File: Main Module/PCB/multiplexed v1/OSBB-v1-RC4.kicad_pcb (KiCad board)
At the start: 2 copper layers, 85.6 x 47.3 mm, 86 parts, among them P1 AUX 0-5V, P14 EXTRA Pins, P2 VUSB, P3 +3.3V, P4 Pit, P5 Encoders, P6 BTN 1-32, Q1 NPN, Q2 NPN, Q3 NPN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

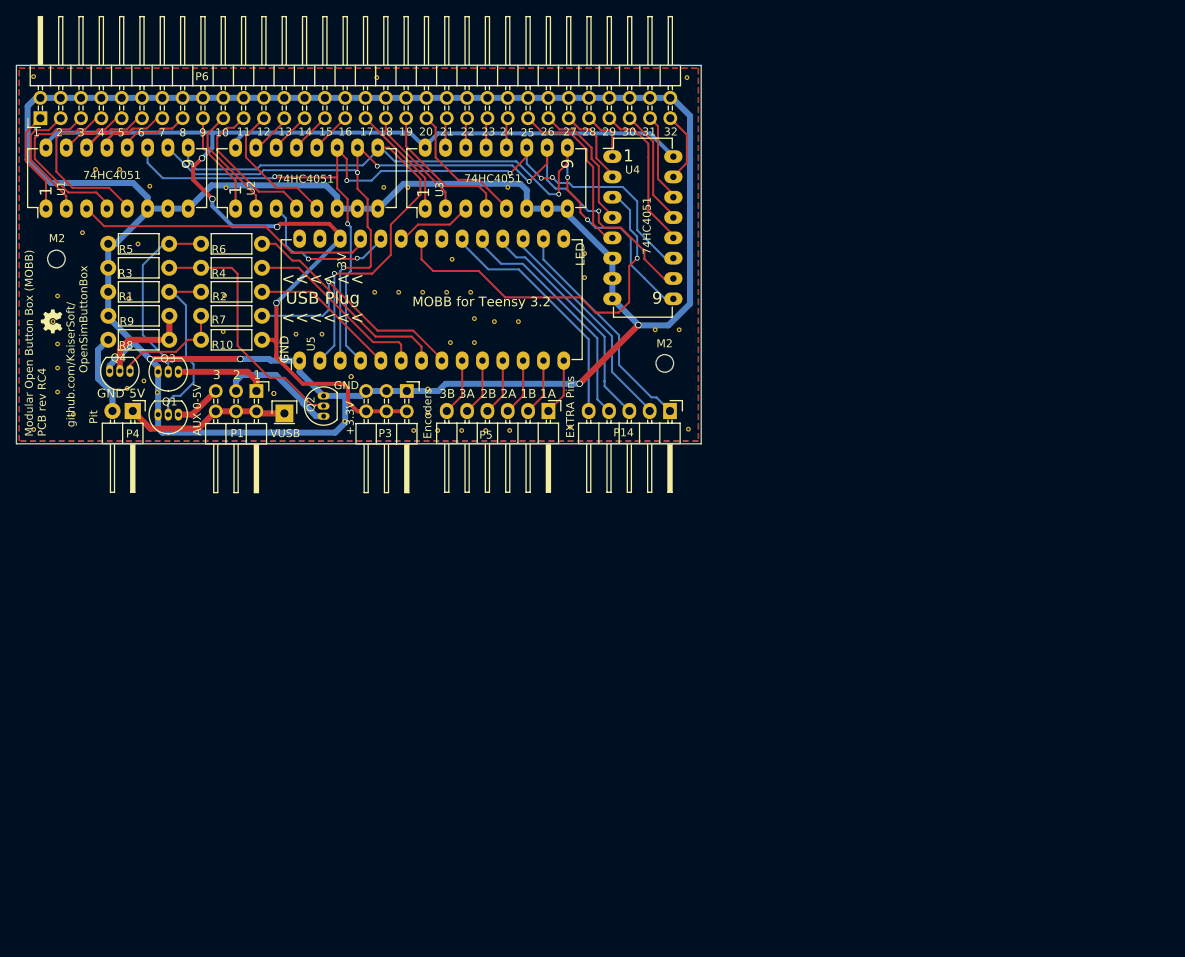
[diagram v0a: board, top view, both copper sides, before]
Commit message: * two tracks to close. had this corrected on Gerber files to manfacturer but did not push it. this is the fix.
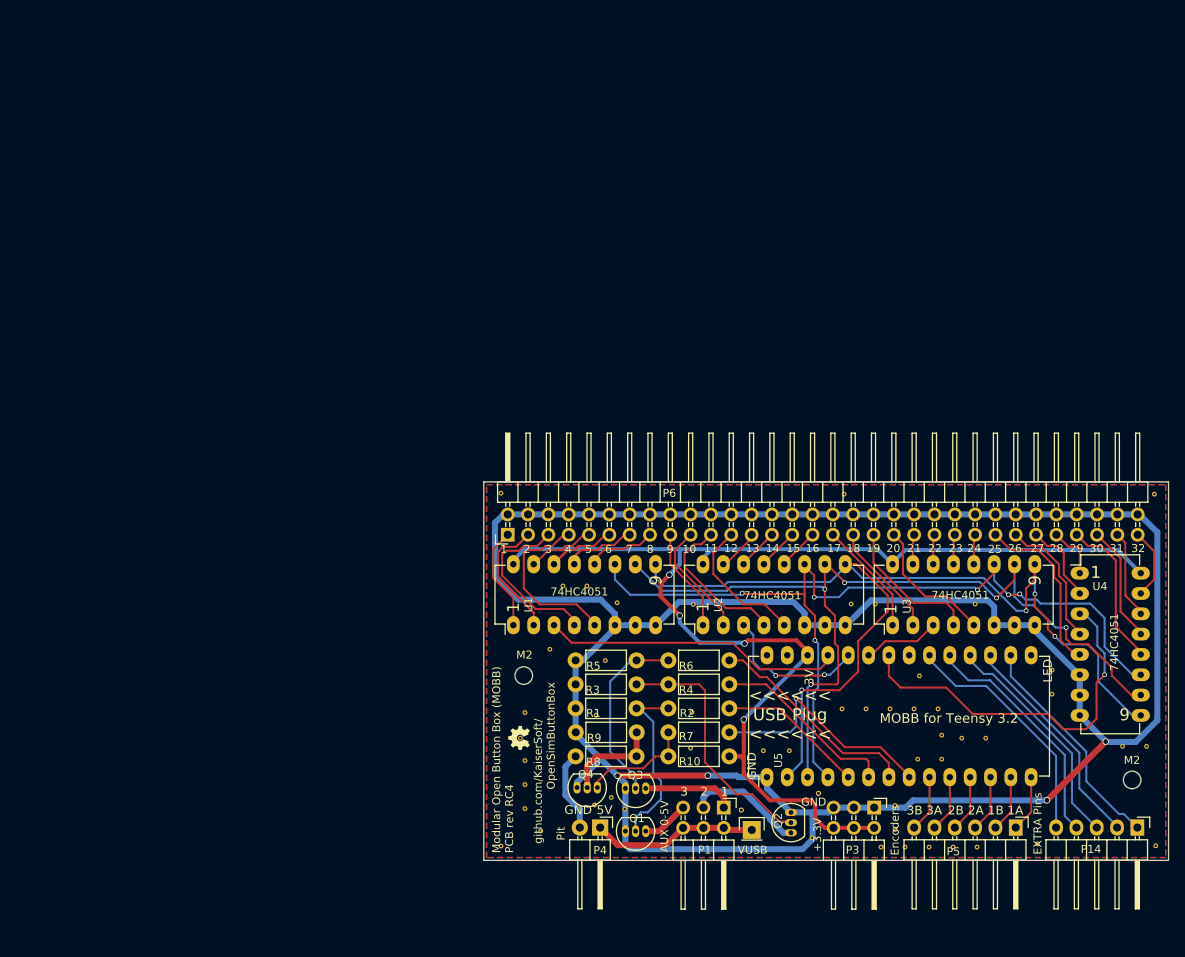
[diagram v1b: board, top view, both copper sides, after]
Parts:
- moved R10 78.3 mm to (206.0, 131.8)
- moved R7 78.3 mm to (206.0, 128.8)
- moved REF** 78.3 mm to (189.4, 126.6)
- moved REF** 78.3 mm to (190.5, 119.8)
- moved REF** 78.3 mm to (220.4, 99.0)
- moved REF** 78.3 mm to (258.2, 130.5)
- moved REF** 78.3 mm to (179.9, 129.5)
- moved U1 78.3 mm to (179.0, 115.4)
- moved P3 78.3 mm to (224.1, 138.2)
- moved P4 78.3 mm to (189.9, 140.7)
- moved Q4 78.3 mm to (189.5, 135.7)
- moved R2 78.3 mm to (206.0, 125.8)
- moved R4 78.3 mm to (206.0, 122.8)
- moved R6 78.3 mm to (206.0, 119.8)
- moved REF** 78.3 mm to (192.9, 138.4)
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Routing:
- net Net-(P6-Pad13): track 12.9 -> 12.0 mm
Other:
- rule trace_min: 0.21 -> 0.25
